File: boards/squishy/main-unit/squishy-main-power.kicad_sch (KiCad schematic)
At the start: 142 parts, among them Q1 NTMFS5C442NT1G, Q2 NX6008NBKR, Q3 NX6008NBKR, Q4 NX6008NBKR, Q5 NX6008NBKR, SW1 RST, U1 LFE5UM5G-45F-8BG381C, U13 LM51551DSSR, U18 HyperRAM, U19 HyperRAM, U2 GD25Q64EWIGR, U21 AP3428/A, U5 APX811-40UG-7, U7 TPS73733DRVR, U8 TPS7A1125PDRVT, U9 TPS7A1112PDRVT

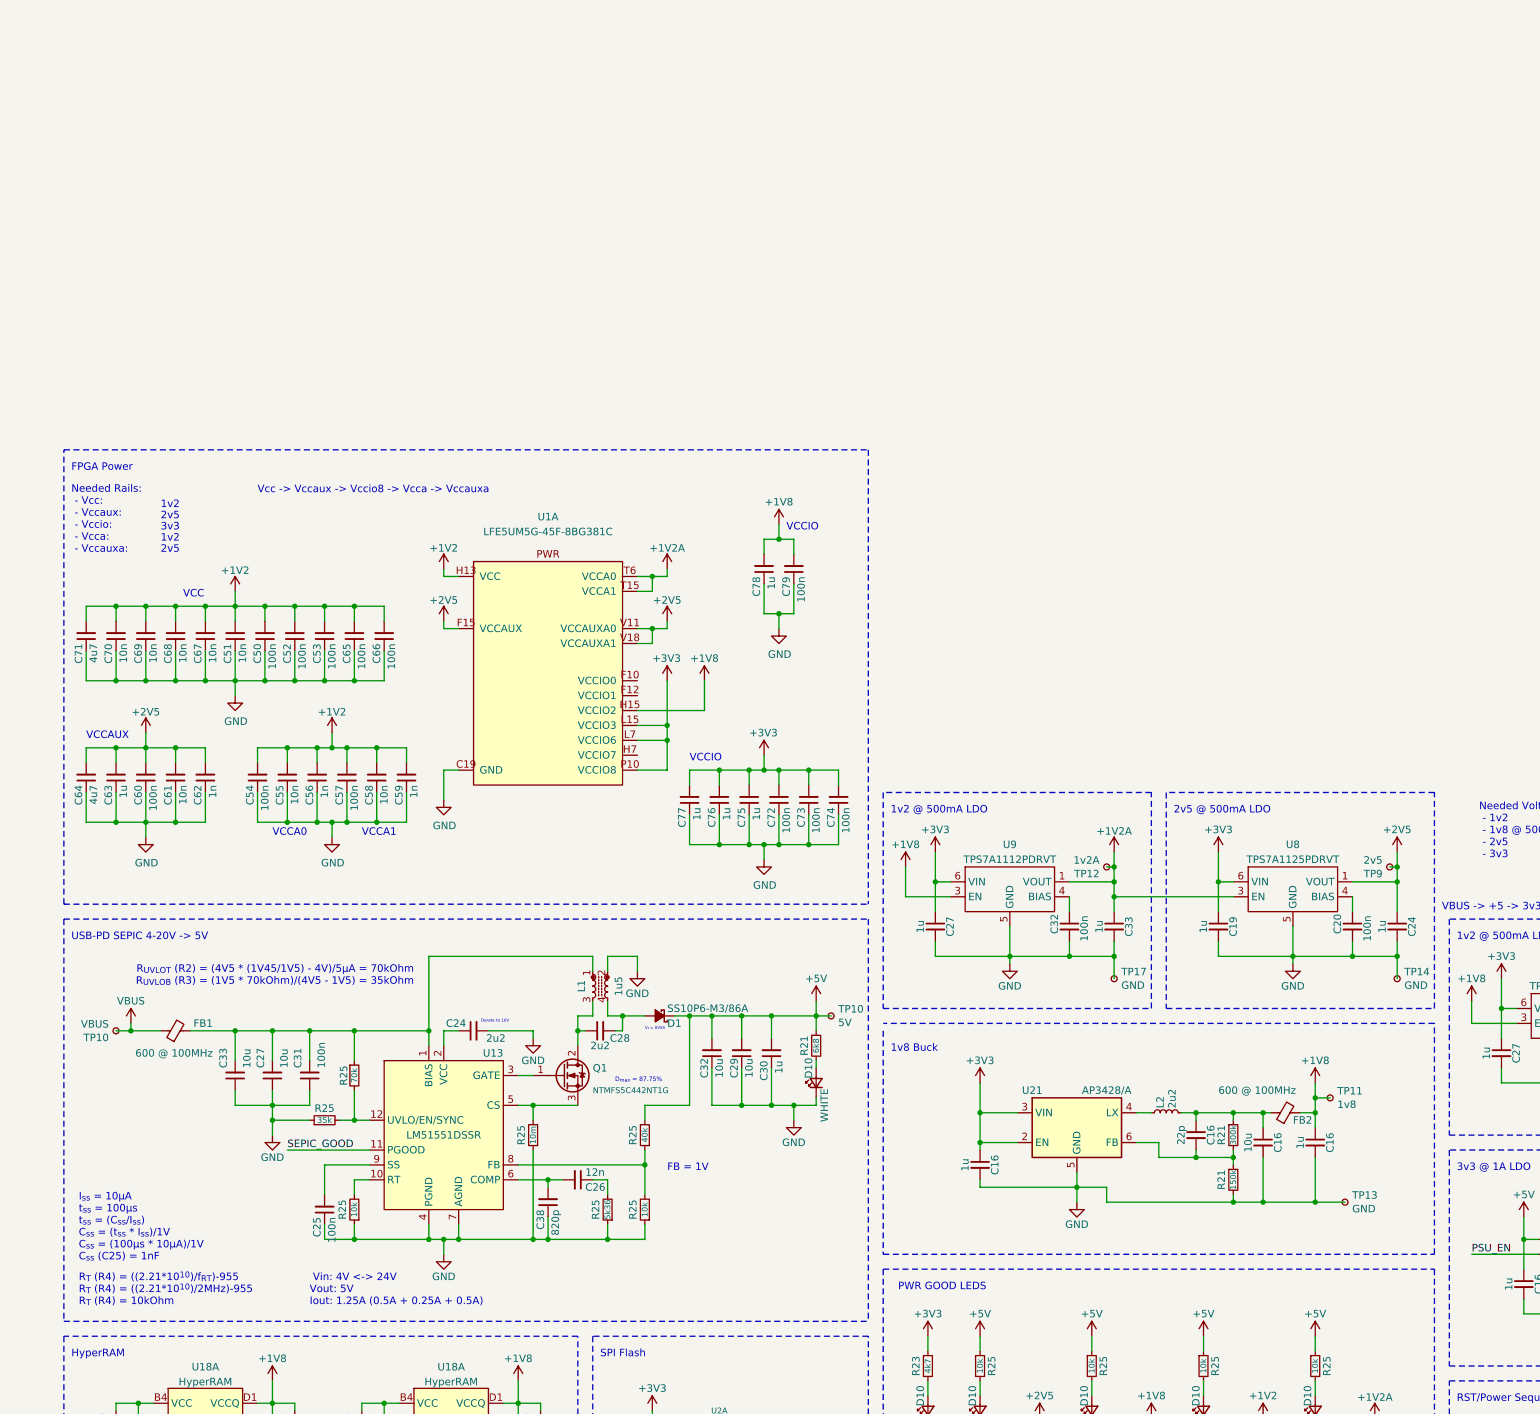
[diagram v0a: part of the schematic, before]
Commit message: squishy: main: More massive rework of the power situation, now with OVP and OCP, as well as if needed supplemental DC jack if USB-PD is not available
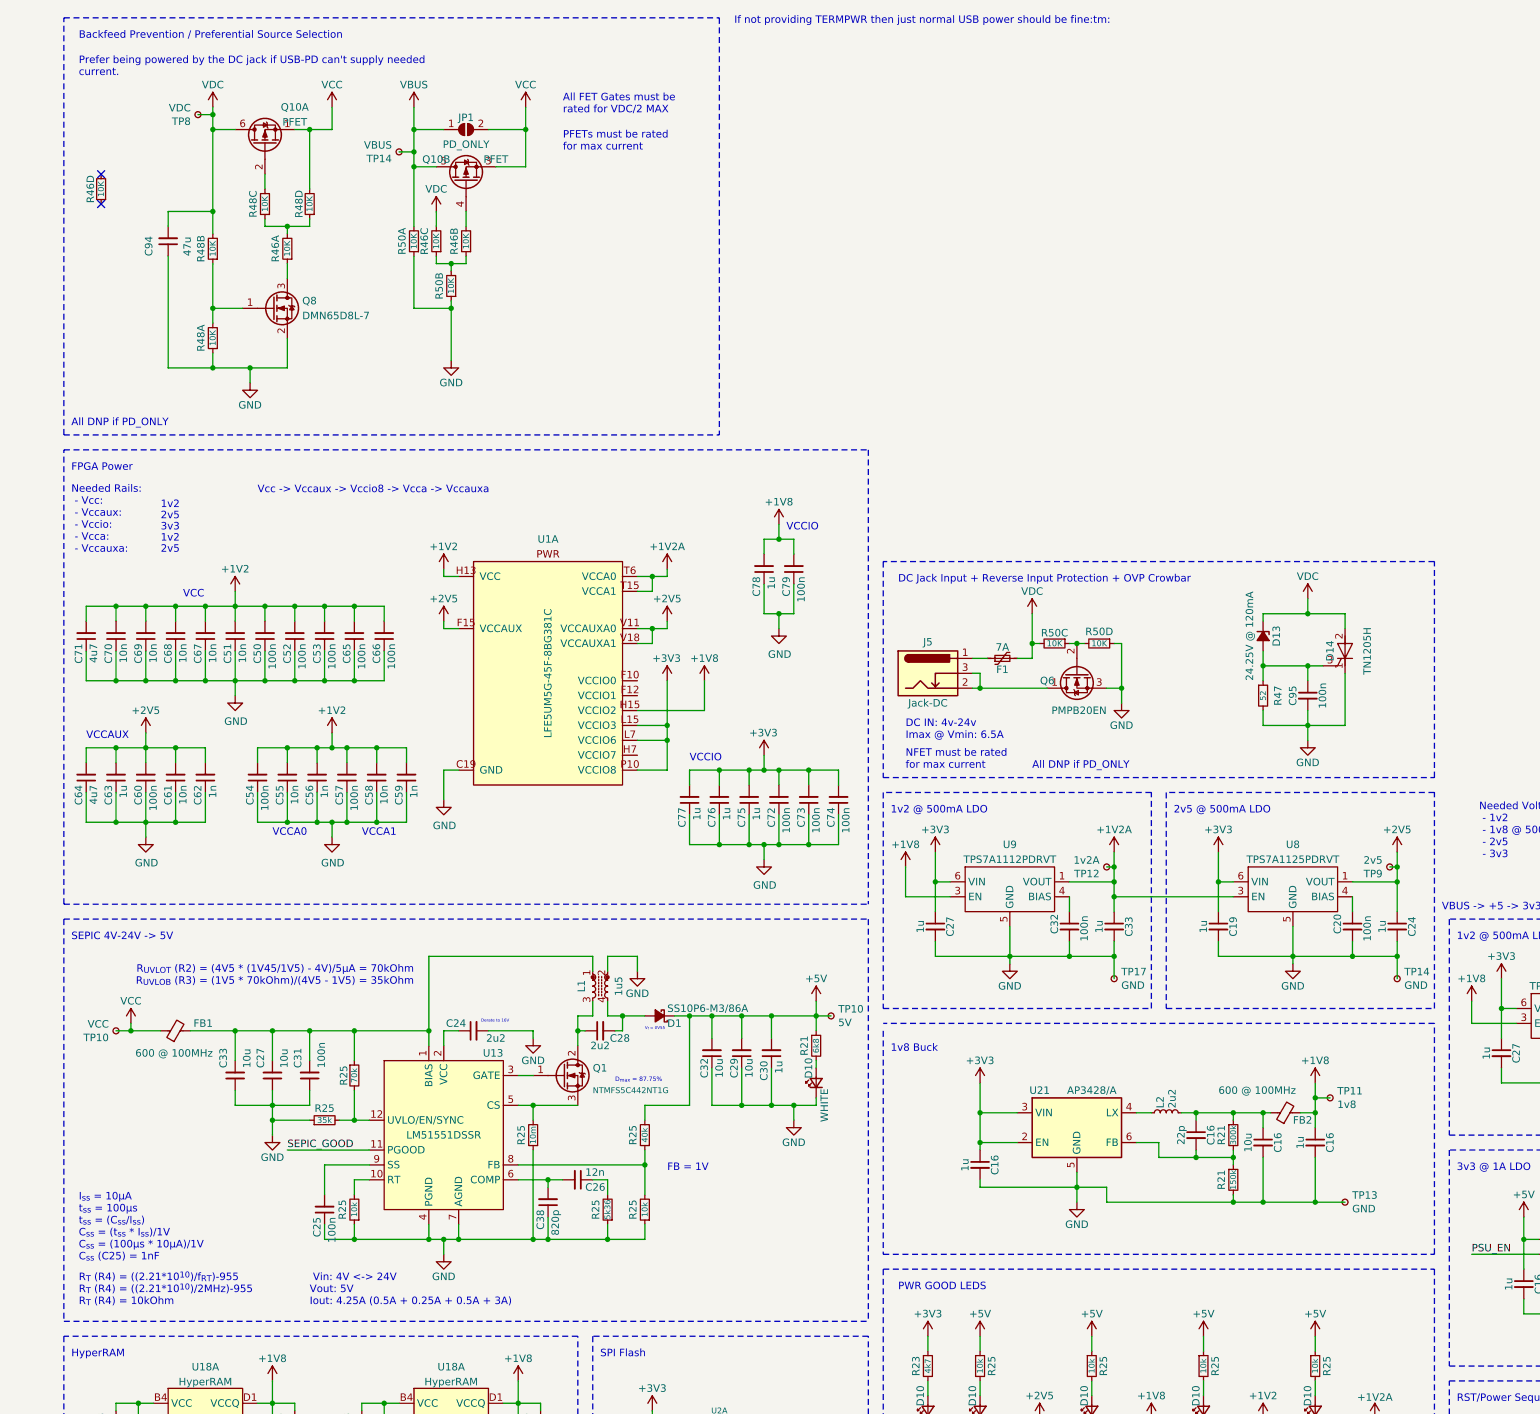
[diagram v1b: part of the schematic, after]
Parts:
- added C94: 47u, Capacitor_SMD:C_0805_2012Metric, symbol Device:C_Small
- added C95: 100n, Capacitor_SMD:C_0603_1608Metric, symbol Device:C_Small
- added D13: 24.25V @ 120mA, Diode_SMD:D_SOD-323, symbol Device:D_Zener_Small_Filled
- added D14: TN1205H, Package_TO_SOT_SMD:TO-263-2, symbol Device:Q_SCR_KAG
- added F1: 7A, Fuse:Fuse_1206_3216Metric, symbol Device:Polyfuse_Small
- added J5: Jack-DC, rhais_connector-jack:BarrelJack_GCT_DCJ200-10-A_Horizontal, symbol Connector:Barrel_Jack_Switch
- added JP1: PD_ONLY, Jumper:SolderJumper-2_P1.3mm_Open_TrianglePad1.0x1.5mm, symbol Jumper:SolderJumper_2_Open
- added Q10: PFET, lethalbit-so:PowerPAK_SO-8L_Dual, symbol lethalbit-devices:Q_Dual_PMOS_S1G1S2G2D2D1
- added Q6: PMPB20EN, lethalbit-so:SOT1220-3, symbol Device:Q_NMOS_DGS
- added Q8: DMN65D8L-7, Package_TO_SOT_SMD:SOT-23, symbol Device:Q_NMOS_GSD
- added R46, R48, R50: 10K, rhais_rcl:R0603_Array_Concave_4, symbol DX-MON:pkl_R4_Small
- added R47: 52, Resistor_SMD:R_0603_1608Metric, symbol Device:R_Small
- added TP14: VBUS, TestPoint:TestPoint_Pad_D1.0mm, symbol Connector:TestPoint_Small
- added TP8: VDC, TestPoint:TestPoint_Pad_D1.0mm, symbol Connector:TestPoint_Small
- D1: footprint Package_TO_SOT_SMD:TO-277A -> lethalbit-so:TO-277A-2
- L1: footprint (none) -> lethalbit-inductor:Bourns-SRF1260; MPN SRF0703-1R5M -> SRF1260-1R5Y
- L2: footprint (none) -> Inductor_SMD:L_0603_1608Metric; MFR (none) -> Abracon LLC; MPN (none) -> AOTA-B160808S2R2MT
- Q1: footprint (none) -> lethalbit-so:ONSemi_SO-8FL_488AA
- R25: footprint (none) -> Resistor_SMD:R_0402_1005Metric
- TP10: value VBUS -> VCC
- renumbered G3 to G4, G2 to G5
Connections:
- net GND: now also C94.1, C95.2, D14.1 (K), Q6.3 (S), Q8.2 (S), R47.2, R48.1, R50.1, R50.3, R50.7
- net VBUS: now also JP1.1 (A), Q10.5 (D), R50.2, TP14.1; no longer FB1.1, TP10.1
- new net: C95.1, D13.2 (A), D14.3 (G), R47.1
- new net: R46.3, R46.5, R50.4
- new net: Q10.4 (G), R46.4
- new net: Q8.3 (D), R46.1
- new net: R46.2, R48.5, R48.7
- new net: Q8.1 (G), R48.2, R48.3
- new net: F1.1, J5.1
- new net: J5.2, J5.3, Q6.1 (D)
- new net: Q10.2 (G), R48.6
- new net: Q6.2 (G), R50.5, R50.8
- new net VCC: FB1.1, JP1.2 (B), Q10.1 (S), Q10.3 (S), R48.8, TP10.1
- new net VDC: C94.2, D13.1 (K), D14.2 (A), F1.2, Q10.6 (D), R46.6, R48.4, R50.6, TP8.1
- no-connect marks 1 -> 3
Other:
- note added: "All DNP if PD_ONLY"
- note added: "All FET Gates must be rated for VDC/2 MAX"
- note added: "Backfeed Prevention / Preferential Source Selection"
- note added: "DC IN: 4v-24v Imax @ Vmin: 6.5A"
- note added: "DC Jack Input + Reverse Input Protection + OVP Crowbar"
- note added: "If not providing TERMPWR then just normal USB power should be fine:tm:"
- note added: "NFET must be rated for max current"
- note added: "PFETs must be rated for max current"
- note added: "Prefer being powered by the DC jack if USB-PD can't supply needed current."
- note added: "SEPIC 4V-24V -> 5V"
- note added: "Vin: 4V <-> 24V Vout: 5V Iout: 4.25A (0.5A + 0.25A + 0.5A + 3A)"
- note removed: "USB-PD SEPIC 4-20V -> 5V"
- note removed: "Vin: 4V <-> 24V Vout: 5V Iout: 1.25A (0.5A + 0.25A + 0.5A)"

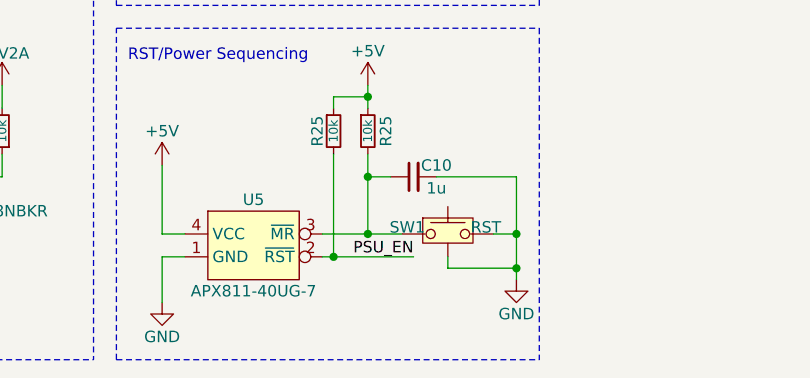
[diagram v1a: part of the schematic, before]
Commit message: squishy: main: Added a whole bunch of test points
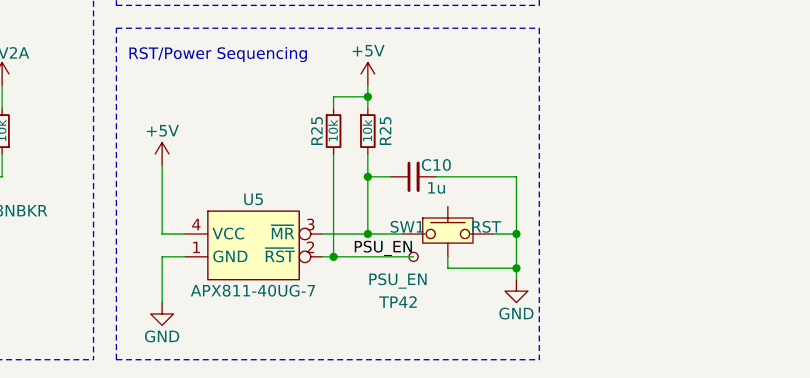
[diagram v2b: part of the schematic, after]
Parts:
- added TP42: PSU_EN, TestPoint:TestPoint_Pad_D1.0mm, symbol Connector:TestPoint_Small
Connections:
- net PSU_EN: now also TP42.1
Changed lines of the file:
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@@
+    )
+  )
+  (symbol (lib_id "Connector:TestPoint_Small") (at 283.21 271.78 270) (unit 1)
+    (in_bom no) (on_board yes) (dnp no)
+    (property "Reference" "TP42" (at 279.4 276.86 90)
+      (effects (font (size 1.27 1.27)) (justify left))
+    )
+    (property "Value" "PSU_EN" (at 278.13 274.32 90)
+      (effects (font (size 1.27 1.27)) (justify left))
+    )
+    (property "Footprint" "TestPoint:TestPoint_Pad_D1.0mm" (at 283.21 276.86 0)
+      (effects (font (size 1.27 1.27)) hide)
+    )
+    (property "Datasheet" "~" (at 283.21 276.86 0)
+      (effects (font (size 1.27 1.27)) hide)
+    )
+    (property "MFR" "N/A" (at 283.21 271.78 0)
+      (effects (font (size 1.27 1.27)) hide)
+    )
+    (property "MPN" "N/A" (at 283.21 271.78 0)
+      (effects (font (size 1.27 1.27)) hide)
+    )
+    (pin "1")
+    (instances
+      (project "squishy-main"
+        (path "/d4567381-92dd-4d3b-8c64-40007ced30aa/3a0401a0-2db0-4f5c-bc8b-66f50b74dd32"
+          (reference "TP42") (unit 1)
+        )
+      )
     )
   )

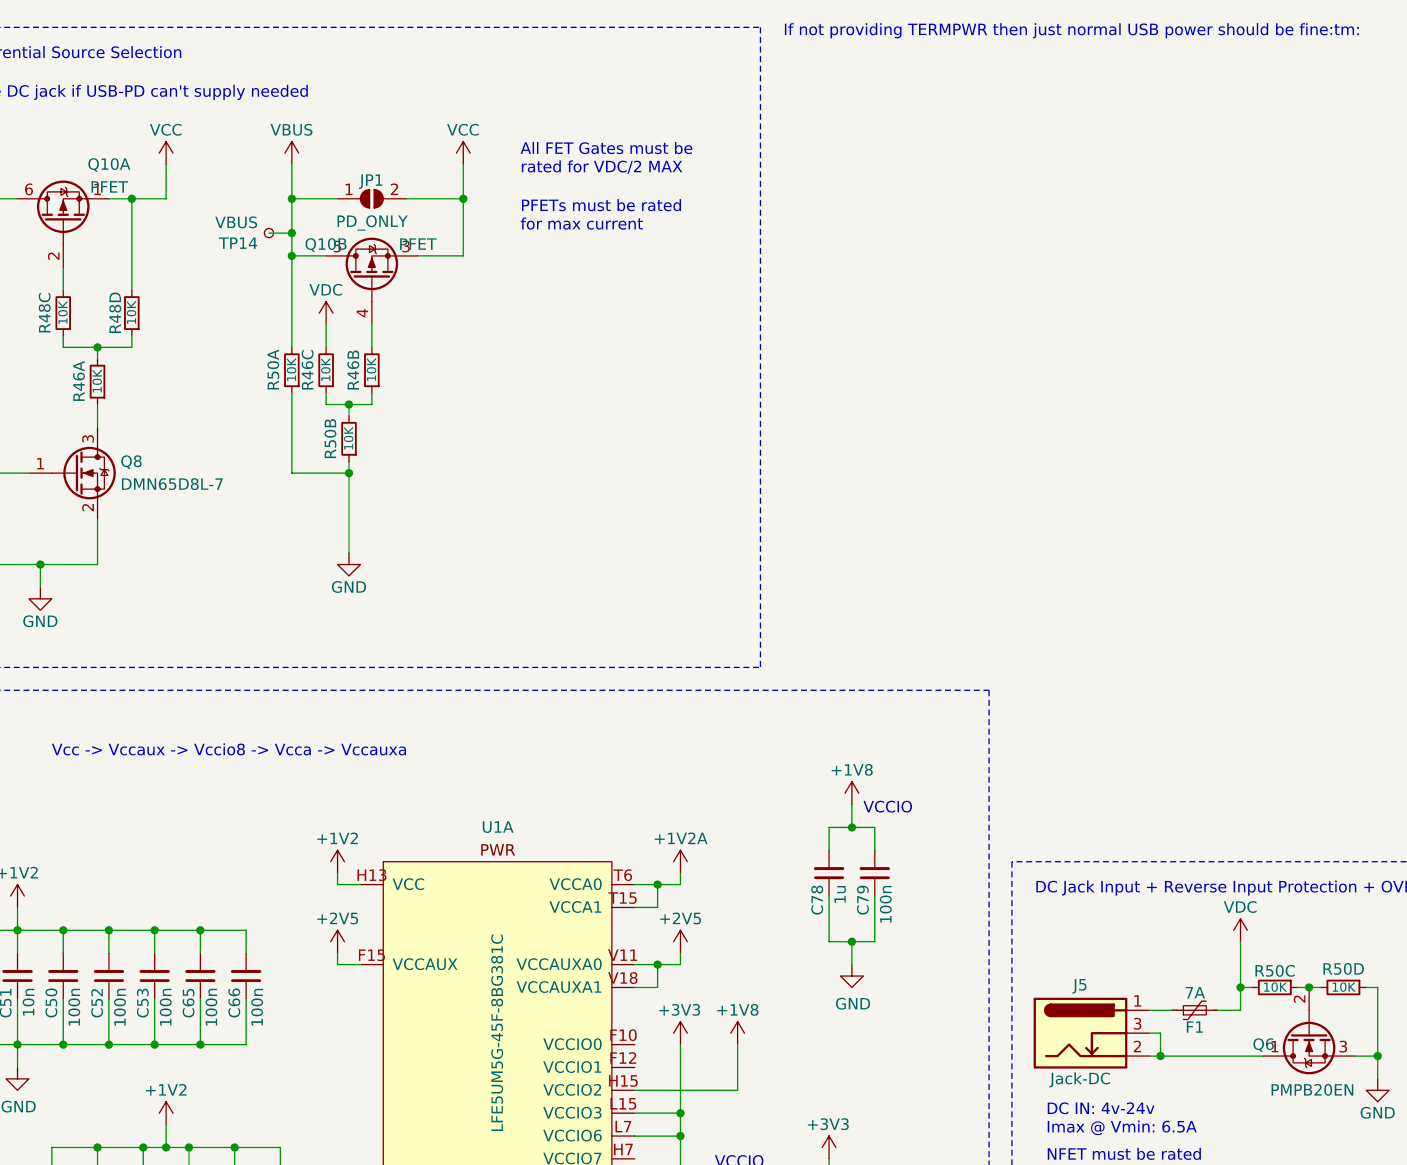
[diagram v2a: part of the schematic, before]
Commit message: squishy: main: Fixed ERC errors on the `VBUS`/`VDC` and `VCC` nets due to the brain scramble that is the new power topology
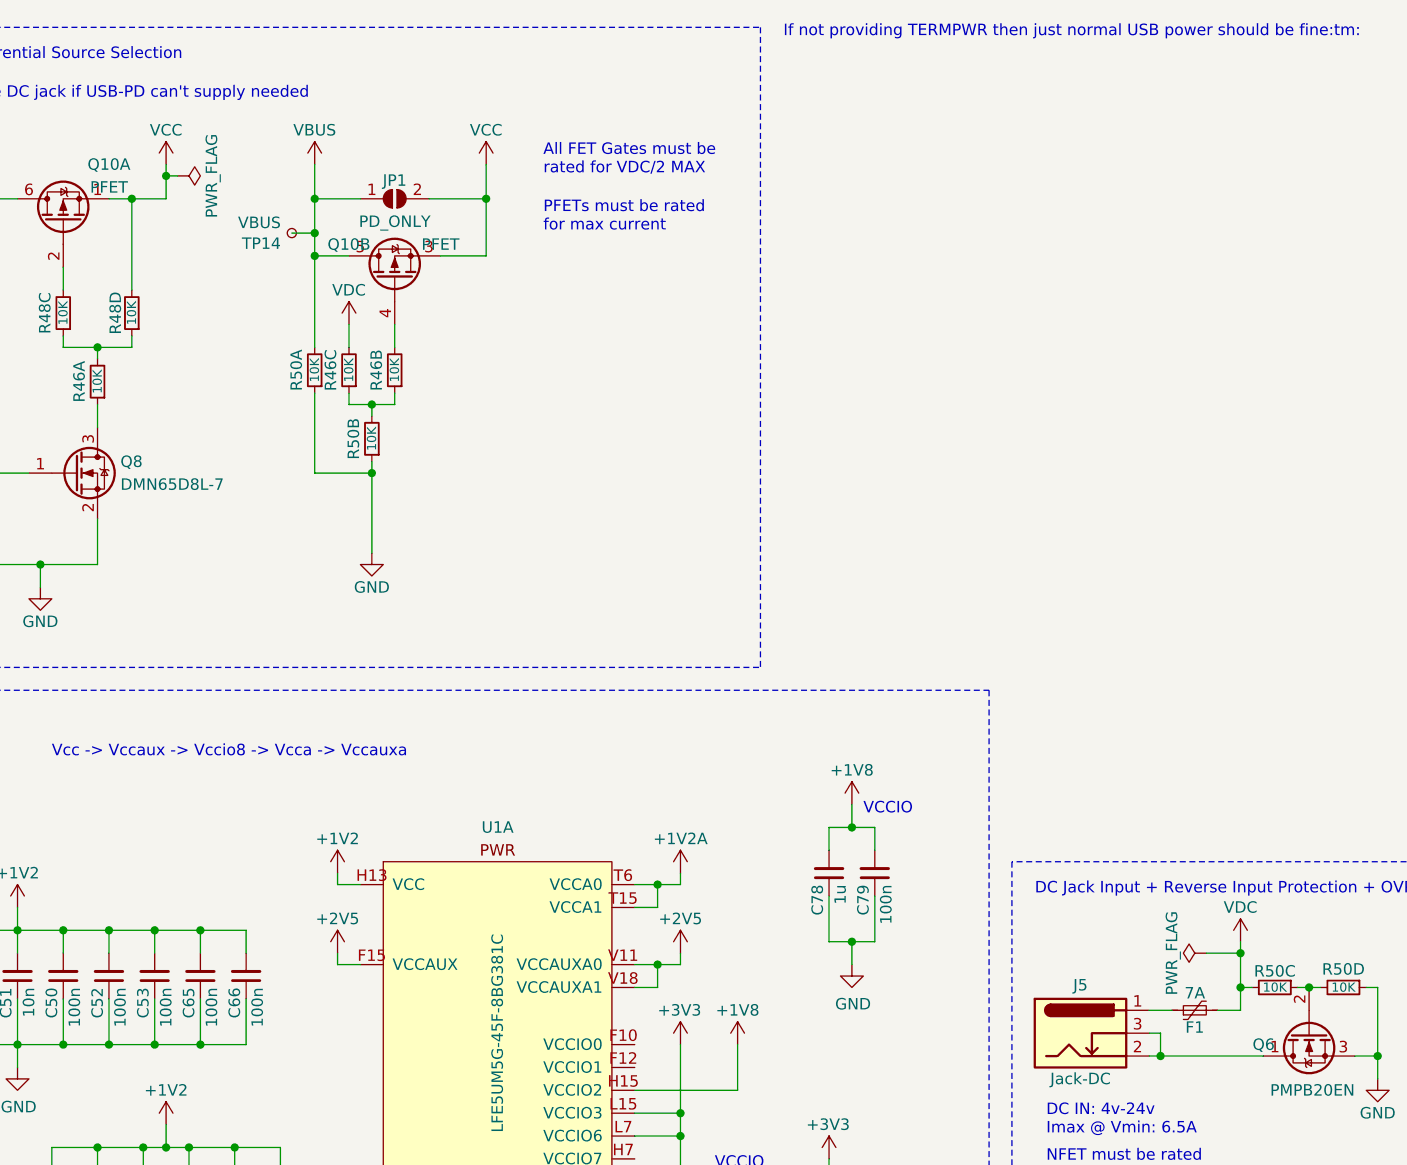
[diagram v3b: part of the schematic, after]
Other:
- moved on the sheet: JP1, Q10B, R46B, R46C, R50A, R50B, TP14
